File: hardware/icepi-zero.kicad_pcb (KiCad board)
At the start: 4 copper layers, 65 x 30 mm, 68 parts, among them J1 Micro_SD_Card_Det2, J2 Conn_02x20_Counter_Clockwise, J3 HDMI_C_1.3, J4 USB_C_Receptacle_USB2.0_14P, J5 USB_C_Receptacle_USB2.0_14P, J6 USB_C_Receptacle_USB2.0_14P, U1 ECP5U_12_CABGA256, U10 TPD2EUSB30A, U11 W25Q128JVS, U2 TLV62569DBV, U3 TLV62569DBV, U4 TLV62569DBV, U5 PCA9306DC1, U6 FT231XQ, U7 W9825G6KH, U8 TPD2EUSB30A, U9 TPD2EUSB30A, Y1 YSO690PR

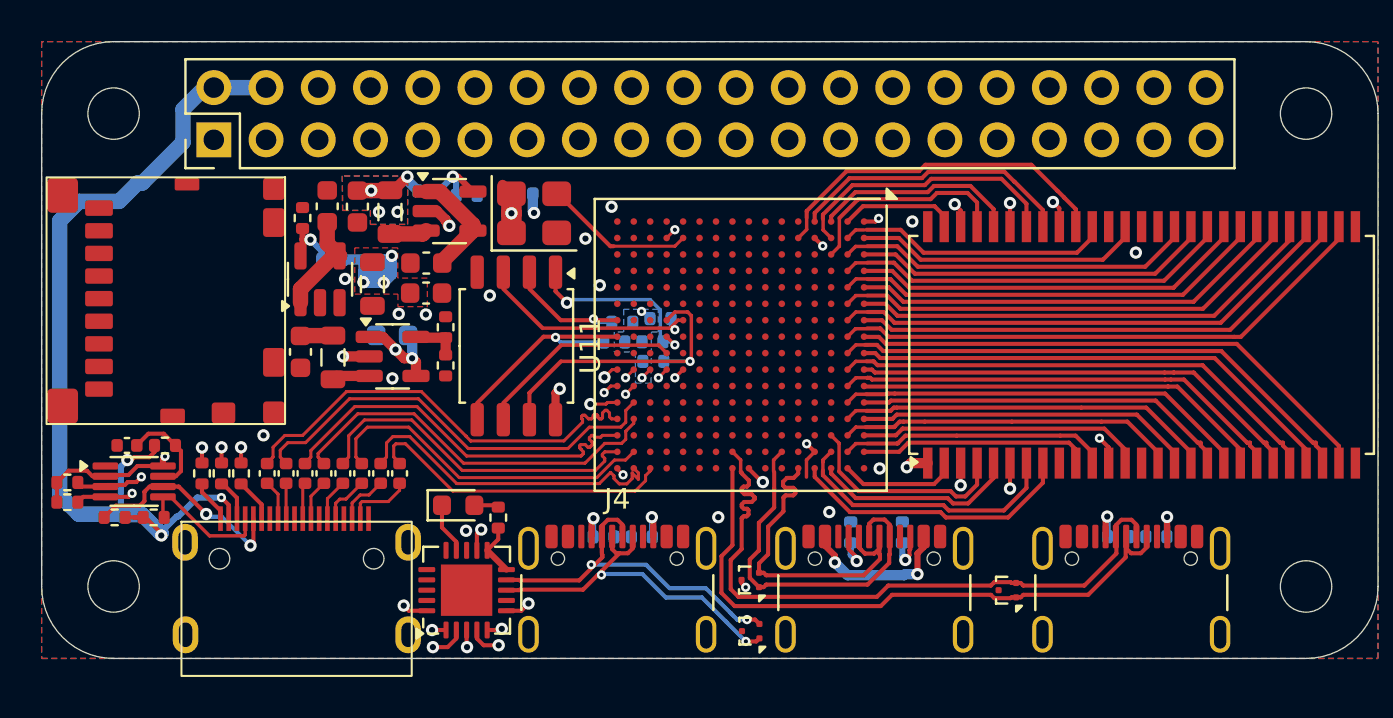
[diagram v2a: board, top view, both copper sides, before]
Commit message: Added the decoupling capacitors
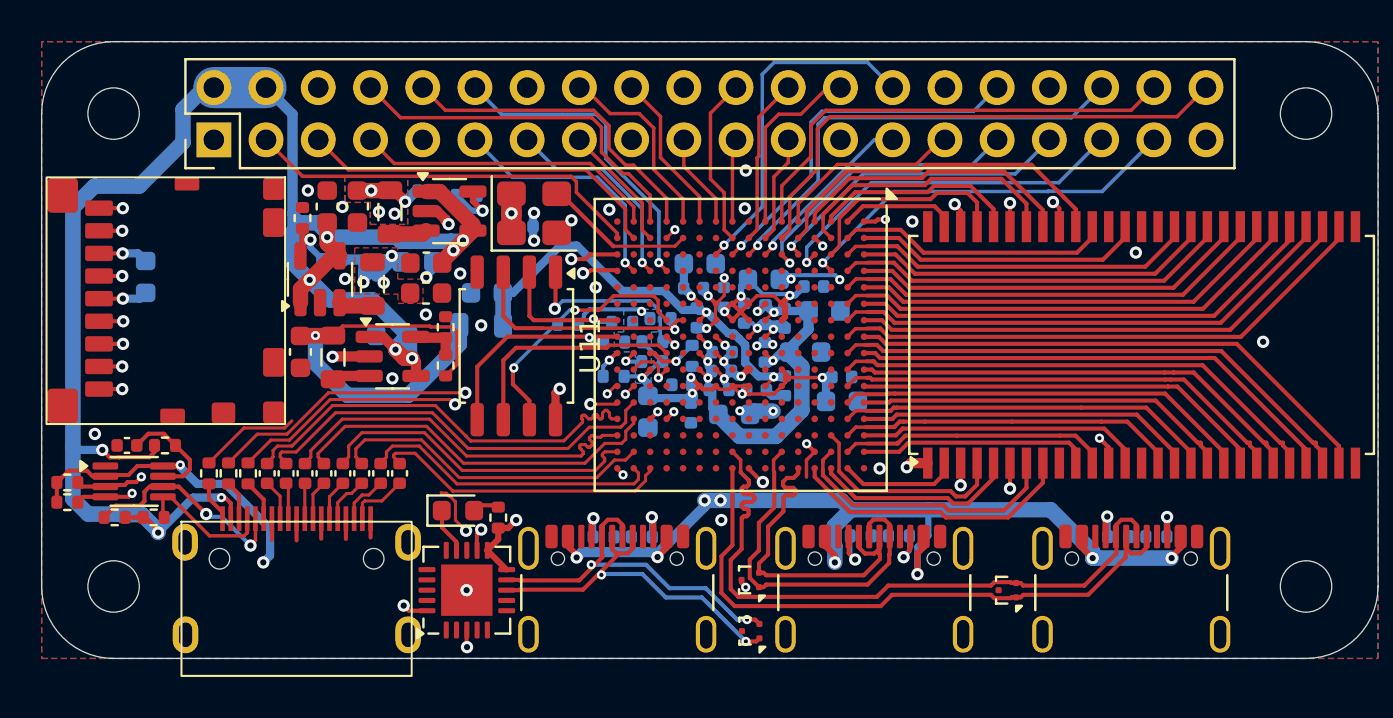
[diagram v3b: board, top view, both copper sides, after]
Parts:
- added C17: 10uF, Capacitor_SMD:C_0603_1608Metric, B.Cu at (137.7, 102.2)
- added C18: 100nF, Capacitor_SMD:C_0402_1005Metric, B.Cu at (152.2, 106.7)
- added C19: 100nF, Capacitor_SMD:C_0402_1005Metric, B.Cu at (147.9, 103.4)
- added C20: 22uF, Capacitor_SMD:C_0603_1608Metric, B.Cu at (134.3, 100.7)
- added C21: 10uF, Capacitor_SMD:C_0603_1608Metric, B.Cu at (154.1, 103.1)
- added C22: 10uF, Capacitor_SMD:C_0603_1608Metric, B.Cu at (153.1, 105.1)
- added C23: 10uF, Capacitor_SMD:C_0603_1608Metric, B.Cu at (149.7, 108.1)
- added C24: 100nF, Capacitor_SMD:C_0402_1005Metric, B.Cu at (152.1, 103.5)
- added C25: 100nF, Capacitor_SMD:C_0402_1005Metric, B.Cu at (151.2, 103.3)
- added C26: 100nF, Capacitor_SMD:C_0402_1005Metric, B.Cu at (151.2, 105.1)
- added C27: 100nF, Capacitor_SMD:C_0402_1005Metric, B.Cu at (148.9, 106.9)
- added C28: 100nF, Capacitor_SMD:C_0402_1005Metric, B.Cu at (149.1, 106.0)
- added C29: 100nF, Capacitor_SMD:C_0402_1005Metric, B.Cu at (149.1, 105.1)
- added C30: 10uF, Capacitor_SMD:C_0603_1608Metric, B.Cu at (145.5, 108.0)
- added C31: 100nF, Capacitor_SMD:C_0402_1005Metric, B.Cu at (147.1, 106.7)
- added C32: 100nF, Capacitor_SMD:C_0402_1005Metric, B.Cu at (147.6, 108.1)
- added C33: 10uF, Capacitor_SMD:C_0603_1608Metric, B.Cu at (148.0, 100.8)
- added C34: 100nF, Capacitor_SMD:C_0402_1005Metric, B.Cu at (147.7, 102.0)
- added C35: 10uF, Capacitor_SMD:C_0603_1608Metric, B.Cu at (151.1, 101.6)
- added C36: 100nF, Capacitor_SMD:C_0402_1005Metric, B.Cu at (149.2, 102.4)
- added C37: 100nF, Capacitor_SMD:C_0402_1005Metric, B.Cu at (153.6, 101.9)
- added C38: 100nF, Capacitor_SMD:C_0402_1005Metric, B.Cu at (150.2, 103.2)
- added C39: 100nF, Capacitor_SMD:C_0402_1005Metric, B.Cu at (154.9, 106.3)
- added C40: 100nF, Capacitor_SMD:C_0402_1005Metric, B.Cu at (150.8, 106.9)
- added C41: 10uF, Capacitor_SMD:C_0603_1608Metric, B.Cu at (154.9, 107.5)
- added C42: 10uF, Capacitor_SMD:C_0603_1608Metric, B.Cu at (121.1, 101.4)
- added FB1: 100R@100MHz, Inductor_SMD:L_0805_2012Metric, B.Cu at (137.4, 103.8)
- added R27: 15k, Resistor_SMD:R_0402_1005Metric, B.Cu at (145.7, 105.6)
- added R28: 15k, Resistor_SMD:R_0402_1005Metric, B.Cu at (147.6, 105.3)
- added R29: 15k, Resistor_SMD:R_0402_1005Metric, B.Cu at (143.8, 106.3)
- C6: value 22uF -> 10uF
- J3: footprint cyao:XKB Connection A71-05H4-111N1 -> icepi-lib:XKB Connection A71-05H4-111N1
- moved R25 4.51 mm to (141.6, 103.8), turned to 180 degrees
- moved C16 1.59 mm to (139.4, 99.0)
- moved R17 0.52 mm to (155.8, 114.0), turned to 0 degrees
- moved R7 0.34 mm to (126.0, 111.0)
- moved R8 0.34 mm to (125.1, 111.0)
- moved R9 0.34 mm to (124.1, 111.0)
- moved D1 0.26 mm to (136.2, 112.8)
- moved R18 0.24 mm to (157.7, 114.0), turned to 0 degrees
- turned L1 to -90 degrees
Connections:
- J1 pad 1: unconnected-(J1-DAT2-Pad1) -> DAT2
- J1 pad 10: unconnected-(J1-DET_A-Pad10) -> DET
- J1 pad 11: unconnected-(J1-SHIELD-Pad11) -> GND
- J1 pad 2: unconnected-(J1-DAT3/CD-Pad2) -> DAT3
- J1 pad 3: unconnected-(J1-CMD-Pad3) -> CMD
- J1 pad 4: unconnected-(J1-VDD-Pad4) -> +3V3
- J1 pad 5: unconnected-(J1-CLK-Pad5) -> CLK
- J1 pad 6: unconnected-(J1-VSS-Pad6) -> GND
- J1 pad 7: unconnected-(J1-DAT0-Pad7) -> DAT0
- J1 pad 8: unconnected-(J1-DAT1-Pad8) -> DAT1
- J1 pad 9: unconnected-(J1-DET_B-Pad9) -> GND
- J2 pad 10: unconnected-(J2-Pin_10-Pad10) -> GPIO_10
- J2 pad 11: unconnected-(J2-Pin_11-Pad11) -> GPIO_11
- J2 pad 12: unconnected-(J2-Pin_12-Pad12) -> GPIO_12
- J2 pad 13: unconnected-(J2-Pin_13-Pad13) -> GPIO_13
- J2 pad 15: unconnected-(J2-Pin_15-Pad15) -> GPIO_15
- J2 pad 16: unconnected-(J2-Pin_16-Pad16) -> GPIO_16
- J2 pad 18: unconnected-(J2-Pin_18-Pad18) -> GPIO_18
- J2 pad 19: unconnected-(J2-Pin_19-Pad19) -> GPIO_19
- J2 pad 21: unconnected-(J2-Pin_21-Pad21) -> GPIO_21
- J2 pad 22: unconnected-(J2-Pin_22-Pad22) -> GPIO_22
- J2 pad 23: unconnected-(J2-Pin_23-Pad23) -> GPIO_23
- J2 pad 24: unconnected-(J2-Pin_24-Pad24) -> GPIO_24
- J2 pad 26: unconnected-(J2-Pin_26-Pad26) -> GPIO_26
- J2 pad 27: unconnected-(J2-Pin_27-Pad27) -> GPIO_27
- J2 pad 28: unconnected-(J2-Pin_28-Pad28) -> GPIO_28
- J2 pad 29: unconnected-(J2-Pin_29-Pad29) -> GPIO_29
- J2 pad 3: unconnected-(J2-Pin_3-Pad3) -> GPIO_3
- J2 pad 31: unconnected-(J2-Pin_31-Pad31) -> GPIO_31
- J2 pad 32: unconnected-(J2-Pin_32-Pad32) -> GPIO_32
- J2 pad 33: unconnected-(J2-Pin_33-Pad33) -> GPIO_33
- J2 pad 35: unconnected-(J2-Pin_35-Pad35) -> GPIO_35
- J2 pad 36: unconnected-(J2-Pin_36-Pad36) -> GPIO_36
- J2 pad 37: unconnected-(J2-Pin_37-Pad37) -> GPIO_37
- J2 pad 38: unconnected-(J2-Pin_38-Pad38) -> GPIO_38
- J2 pad 40: unconnected-(J2-Pin_40-Pad40) -> GPIO_40
- J2 pad 5: unconnected-(J2-Pin_5-Pad5) -> GPIO_5
- J2 pad 7: unconnected-(J2-Pin_7-Pad7) -> GPIO_7
- J2 pad 8: unconnected-(J2-Pin_8-Pad8) -> GPIO_8
- U1 pad C4: unconnected-(U1B-PT11A/+-PadC4) -> GPIO_37
- U1 pad D3: unconnected-(U1G-PL2D/-/LDQ8-PadD3) -> GPIO_35
- U1 pad E1: unconnected-(U1G-PL11D/-/LDQ8-PadE1) -> GPIO_29
- U1 pad E3: unconnected-(U1G-PL5C/+/LDQ8-PadE3) -> GPIO_33
- U1 pad F1: unconnected-(U1G-PL14A/+/HS/LDQ20-PadF1) -> GPIO_38
- U1 pad F10: Net-(U1C-VCCIO1[2]-PadF10) -> +3V3
- U1 pad F11: Net-(U1C-VCCIO1[2]-PadF10) -> +3V3
- U1 pad F2: unconnected-(U1G-PL11C/+/LDQ8-PadF2) -> GPIO_40
- U1 pad F3: unconnected-(U1G-PL5D/-/LDQ8-PadF3) -> GPIO_31
- U1 pad F6: Net-(U1B-VCCIO0[2]-PadF6) -> +3V3
- U1 pad F7: Net-(U1B-VCCIO0[2]-PadF6) -> +3V3
- U1 pad G1: unconnected-(U1G-PL20A/+/GR_PCLK7_1/HS/LDQS20-PadG1) -> GPIO_26
- U1 pad G2: unconnected-(U1G-PL14B/-/HS/LDQ20-PadG2) -> GPIO_23
- U1 pad G3: unconnected-(U1G-PL14C/+/VREF1_7/LDQ20-PadG3) -> GPIO_27
- U1 pad G6: Net-(U1A-VCC[6]-PadG6) -> +1V1
- U1 pad G7: Net-(U1A-VCC[6]-PadG6) -> +1V1
- U1 pad G9: Net-(U1A-VCC[6]-PadG6) -> +1V1
- U1 pad H11: Net-(U1D-VCCIO2[2]-PadH11) -> +3V3
- U1 pad H2: unconnected-(U1G-PL20B/-/HS/LDQSN20-PadH2) -> GPIO_24
- U1 pad H3: unconnected-(U1G-PL14D/-/LDQ20-PadH3) -> GPIO_36
- U1 pad H6: Net-(U1G-VCCIO7[2]-PadH6) -> +3V3
- U1 pad H7: Net-(U1G-VCCIO7[2]-PadH6) -> +3V3
- U1 pad J1: unconnected-(U1G-PL23A/+/PCLKT7_1/HS/LDQ20-PadJ1) -> GPIO_21
- U1 pad J11: Net-(U1D-VCCIO2[2]-PadH11) -> +3V3
- U1 pad J2: unconnected-(U1G-PL23B/-/PCLKC7_1/HS/LDQ20-PadJ2) -> GPIO_22
- U1 pad J3: unconnected-(U1G-PL20C/+/GR_PCLK7_0/LDQ20-PadJ3) -> GPIO_32
- U1 pad J6: Net-(U1F-VCCIO6[2]-PadJ6) -> +3V3
- U1 pad J7: Net-(U1F-VCCIO6[2]-PadJ6) -> +3V3
- U1 pad K1: unconnected-(U1G-PL23C/+/PCLKT7_0/LDQ20-PadK1) -> GPIO_19
- U1 pad K11: Net-(U1E-VCCIO3[2]-PadK11) -> +3V3
- U1 pad K3: unconnected-(U1G-PL20D/-/LDQ20-PadK3) -> GPIO_28
- U1 pad L1: unconnected-(U1F-PL26A/+/PCLKT6_1/HS/LDQ32-PadL1) -> GPIO_18
- U1 pad L10: Net-(U1A-VCC[6]-PadG6) -> +1V1
- U1 pad L11: Net-(U1E-VCCIO3[2]-PadK11) -> +3V3
- U1 pad L6: unconnected-(U1H-VCCIO8-PadL6) -> +3V3
- U1 pad L8: Net-(U1A-VCC[6]-PadG6) -> +1V1
- U1 pad L9: Net-(U1A-VCC[6]-PadG6) -> +1V1
- U1 pad M1: unconnected-(U1F-PL26C/+/PCLKT6_0/LDQ32-PadM1) -> GPIO_16
- U1 pad N1: unconnected-(U1F-PL32A/+/HS/LDQS32-PadN1) -> GPIO_10
- U1 pad N4: unconnected-(U1F-PL38A/+/HS/LDQ44-PadN4) -> GPIO_12
- U1 pad P1: unconnected-(U1F-PL35A/+/HS/LDQ32-PadP1) -> GPIO_8
- U1 pad P2: unconnected-(U1F-PL32B/-/HS/LDQSN32-PadP2) -> GPIO_15
- U1 pad P4: unconnected-(U1F-PL41A/+/HS/LDQ44-PadP4) -> GPIO_13
- U1 pad P9: unconnected-(U1H-DONE-PadP9) -> DONE
- U1 pad R1: unconnected-(U1F-PL35B/-/VREF1_6/HS/LDQ32-PadR1) -> GPIO_7
- U1 pad R2: unconnected-(U1F-PL38C/+/LDQ44-PadR2) -> GPIO_5
- U1 pad R4: unconnected-(U1F-PL41C/+/LDQ44-PadR4) -> GPIO_11
- U1 pad R9: unconnected-(U1H-PROGRAMN-PadR9) -> PROGRAMMING
- U1 pad T2: unconnected-(U1F-PL38D/-/LDQ44-PadT2) -> GPIO_3
- U1 pad T3: unconnected-(U1F-PL41D/-/LDQ44-PadT3) -> FPDI_SCL
- U1 pad T4: unconnected-(U1F-PL44B/-/HS/LDQSN44-PadT4) -> FPDI_SDA
- U1 pad T9: unconnected-(U1H-INITN-PadT9) -> INITN
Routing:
- net +5V: track 68.9 -> 200.2 mm, vias 8 -> 18
- net +1V1: track 10.2 -> 61.4 mm, vias 3 -> 9
- net +3V3: track 19.8 -> 66.6 mm, vias 12 -> 22
- net GND: track 18.0 -> 51.2 mm, vias 33 -> 55
- net GPIO_40: track 0.00 -> 25.8 mm
- net GPIO_38: track 0.00 -> 22.7 mm
- net GPIO_36: track 0.00 -> 22.3 mm, vias 0 -> 1
- net Net-(C17-Pad1): track 0.00 -> 21.3 mm, vias 0 -> 2
- net +2V5: track 1.59 -> 21.2 mm, vias 0 -> 1
- net GPIO_3: track 0.00 -> 19.5 mm
- net GPIO_37: track 0.00 -> 19.2 mm, vias 0 -> 1
- net GPIO_5: track 0.00 -> 17.9 mm
- net GPIO_35: track 0.00 -> 17.8 mm, vias 0 -> 1
- net GPIO_32: track 0.00 -> 17.8 mm, vias 0 -> 1
- net GPIO_8: track 0.00 -> 17.8 mm
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
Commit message: V1.0 Final Revision and Readme documentation
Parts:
- added C30: 100nF, Capacitor_SMD:C_0402_1005Metric, F.Cu at (179.8, 112.0)
- added C31: 100nF, Capacitor_SMD:C_0402_1005Metric, B.Cu at (168.6, 111.2)
- added C32: 100nF, Capacitor_SMD:C_0402_1005Metric, B.Cu at (166.7, 111.2)
- added C33: 10uF, Capacitor_SMD:C_0603_1608Metric, B.Cu at (161.9, 110.4)
- added C34: 100nF, Capacitor_SMD:C_0402_1005Metric, B.Cu at (161.9, 111.6)
- added C35: 100nF, Capacitor_SMD:C_0402_1005Metric, F.Cu at (169.1, 97.5)
- added D1: WHITE, LED_SMD:LED_0603_1608Metric, F.Cu at (168.2, 112.2)
- added D2: WHITE, LED_SMD:LED_0603_1608Metric, F.Cu at (174.1, 112.2)
- added D3: WHITE, LED_SMD:LED_0603_1608Metric, F.Cu at (177.1, 112.2)
- added D4: WHITE, LED_SMD:LED_0603_1608Metric, F.Cu at (171.1, 112.3)
- added G***: LOGO, LOGO, B.Cu at (178.1, 99.0)
- added R1: 470, Resistor_SMD:R_0402_1005Metric, B.Cu at (168.3, 112.3)
- added R2: 470, Resistor_SMD:R_0402_1005Metric, B.Cu at (174.6, 112.2)
- added R3: 470, Resistor_SMD:R_0402_1005Metric, B.Cu at (177.2, 112.2)
- added R4: 470, Resistor_SMD:R_0402_1005Metric, B.Cu at (171.4, 112.2)
- added TP1: TestPoint, TestPoint:TestPoint_Pad_D2.0mm, B.Cu at (117.9, 107.6)
- added TP2: TestPoint, TestPoint:TestPoint_Pad_D2.0mm, B.Cu at (132.6, 97.8)
- added TP3: TestPoint, TestPoint:TestPoint_Pad_D2.0mm, B.Cu at (128.8, 105.2)
- added TP4: TestPoint, TestPoint:TestPoint_Pad_D2.0mm, B.Cu at (173.8, 101.6)
- added TP5: TestPoint, TestPoint:TestPoint_Pad_D2.0mm, B.Cu at (129.1, 115.5)
- added TP6: TestPoint, TestPoint:TestPoint_Pad_D2.0mm, B.Cu at (136.6, 106.2)
- added TP7: TestPoint, TestPoint:TestPoint_Pad_D2.0mm, B.Cu at (153.9, 117.5)
- added TP8: TestPoint, TestPoint:TestPoint_Pad_D2.0mm, B.Cu at (144.9, 118.1)
- C13: renamed from C3; moved to F.Cu
- C3: renamed from C20; moved to F.Cu
- R6: renamed from R2; moved to B.Cu
- R8: renamed from R4; moved to B.Cu
- Y1: value YSO690PR -> SIT8008xx-1x-xxE-100.000000; footprint Oscillator:Oscillator_SMD_SiT_PQFN-4Pin_3.2x2.5mm -> Oscillator:Oscillator_SMD_SiT_PQFN-4Pin_2.5x2.0mm
- moved C3 7.47 mm to (129.1, 106.1), turned to 180 degrees
- moved C2 6.07 mm to (129.1, 104.6), turned to 180 degrees
- moved C14 5.82 mm to (134.3, 106.3), turned to 0 degrees
- moved R6 5.03 mm to (126.7, 103.2), turned to 180 degrees
- moved R8 4.21 mm to (131.9, 105.8)
- moved C13 3.89 mm to (134.7, 100.8)
- moved R7 3.86 mm to (131.8, 106.4), turned to 180 degrees
- moved R5 3.02 mm to (128.6, 103.2)
- moved L1 3.01 mm to (129.3, 103.0), turned to 0 degrees
- moved C18 2.75 mm to (132.0, 101.0), turned to -90 degrees
- moved R33 2.29 mm to (141.8, 105.2), turned to -90 degrees
- moved U2 2.25 mm to (134.5, 103.6), turned to -90 degrees
- moved L2 2.12 mm to (131.9, 104.2), turned to -90 degrees
- moved U1 1.47 mm to (129.5, 100.1)
- moved R24 1.21 mm to (169.5, 115.0), turned to 90 degrees
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- renumbered C27 to C10, C28 to C11, C29 to C12, C4 to C14, C17 to C15, C18 to C16, C19 to C17, C5 to C18, C6 to C19, C16 to C20, C7 to C21, C8 to C22, C9 to C23, C10 to C24, C11 to C25, C12 to C26, C13 to C27, C14 to C28, C15 to C29, C33 to C36, C34 to C37, C42 to C38, C38 to C39, C23 to C4, C41 to C40, C39 to C41, C37 to C42, C40 to C43, C30 to C44, C31 to C45, C32 to C46, C35 to C47, C36 to C48, C22 to C5, C21 to C6, C24 to C7, C25 to C8, C26 to C9, D1 to D5, J2 to J1, J3 to J2, J4 to J3, J6 to J4, J1 to J6, R6 to R10, R10 to R11, R11 to R12, R12 to R13, R13 to R14, R14 to R15, R7 to R16, R8 to R17, R9 to R18, R15 to R19, R16 to R20, R19 to R22, R17 to R23, R20 to R24, R18 to R25, R22 to R26, R23 to R27, R24 to R28, R25 to R29, R26 to R30, R27 to R31, R28 to R32, R29 to R33, R1 to R5, R3 to R7, R5 to R9, U2 to U1, U7 to U10, U3 to U2, U1 to U3, U8 to U7, U10 to U8
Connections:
- net Net-(C17-Pad1) renamed /Power/FILTERED_2V5
- J6 pad 1: DAT2 -> SD_DAT2
- J6 pad 10: DET -> SD_DET
- J6 pad 2: DAT3 -> SD_DAT3
- J6 pad 3: CMD -> SD_CMD
- J6 pad 5: CLK -> SD_CLK
- J6 pad 7: DAT0 -> SD_DAT0
- J6 pad 8: DAT1 -> SD_DAT1
- U3 pad C13: unconnected-(U1C-PT60B/--PadC13) -> LED3
- U3 pad D14: unconnected-(U1D-PR2D/-/RDQ8-PadD14) -> LED2
- U3 pad E15: unconnected-(U1D-PR8B/-/HS/RDQSN8-PadE15) -> LED4
- U3 pad F16: unconnected-(U1D-PR14A/+/HS/RDQ20-PadF16) -> LED1
- U3 pad K15: unconnected-(U1D-PR23D/-/PCLKC2_0/RDQ20-PadK15) -> USB_RXD
- U3 pad K16: unconnected-(U1D-PR23C/+/PCLKT2_0/RDQ20-PadK16) -> USB_TXD
- U3 pad L14: unconnected-(U1E-PR32C/+/RDQ32-PadL14) -> FPDI_HPD
- U3 pad L15: unconnected-(U1E-PR26B/-/PCLKC3_1/HS/RDQ32-PadL15) -> ~{USB_DTR}
- U3 pad L16: unconnected-(U1E-PR26A/+/PCLKT3_1/HS/RDQ32-PadL16) -> ~{USB_RTS}
- U3 pad M14: unconnected-(U1E-PR32D/-/RDQ32-PadM14) -> SD_DAT3
- U3 pad M15: unconnected-(U1E-PR26D/-/PCLKC3_0/RDQ32-PadM15) -> SD_DAT2
- U3 pad M16: unconnected-(U1E-PR26C/+/PCLKT3_0/RDQ32-PadM16) -> SD_DET
- U3 pad N16: unconnected-(U1E-PR32A/+/HS/RDQS32-PadN16) -> SD_CLK
- U3 pad P14: unconnected-(U1E-PR38B/-/HS/RDQ44-PadP14) -> SD_DAT0
- U3 pad P15: unconnected-(U1E-PR32B/-/HS/RDQSN32-PadP15) -> SD_CMD
- U3 pad P3: unconnected-(U1F-PL38B/-/HS/LDQ44-PadP3) -> GPIO_13
- U3 pad P4: GPIO_13 -> unconnected-(U3F-PL41A/+/HS/LDQ44-PadP4)
- U3 pad P5: unconnected-(U1F-PL47D/-/LLC_GPLL0C_IN/LDQ44-PadP5) -> FPDI_UTIL
- U3 pad R14: unconnected-(U1E-PR41B/-/HS/RDQ44-PadR14) -> SD_DAT1
- U3 pad R3: unconnected-(U1F-PL41B/-/HS/LDQ44-PadR3) -> GPIO_11
- U3 pad R4: GPIO_11 -> unconnected-(U3F-PL41C/+/LDQ44-PadR4)
- U3 pad R5: unconnected-(U1F-PL44A/+/HS/LDQS44-PadR5) -> FPDI_CEC
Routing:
- net SD_DAT0: track 0.00 -> 35.9 mm, vias 0 -> 2
- net SD_DAT1: track 0.00 -> 35.3 mm, vias 0 -> 2
- net SD_CLK: track 0.00 -> 34.5 mm, vias 0 -> 2
- net JTAG_TCK: track 0.00 -> 33.9 mm, vias 0 -> 2
- net SD_DAT3: track 0.00 -> 33.5 mm, vias 0 -> 2
- net FPDI_SDA: track 4.56 -> 37.8 mm, vias 2 -> 4
- net SD_DAT2: track 0.00 -> 32.9 mm, vias 0 -> 2
- net FPDI_SCL: track 5.70 -> 38.3 mm, vias 2 -> 4
- net SD_DET: track 0.00 -> 32.4 mm, vias 0 -> 2
- net SD_CMD: track 0.00 -> 31.9 mm, vias 0 -> 2
- net JTAG_TMS: track 0.65 -> 32.3 mm, vias 1 -> 3
- net JTAG_TDI: track 0.58 -> 31.2 mm, vias 1 -> 2
- net +3V3: track 66.6 -> 93.0 mm, vias 22 -> 25
- net USB_TXD: track 0.00 -> 25.2 mm, vias 0 -> 2
- net LED3: track 0.00 -> 24.8 mm, vias 0 -> 1
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- added copper zone on In2.Cu, net +1V1
- added copper zone on B.Cu, net +2V5
- added copper zone on F.Cu, net +2V5
- added copper zone on In2.Cu, net +5V
- added copper zone on B.Cu, net /Power/FILTERED_2V5

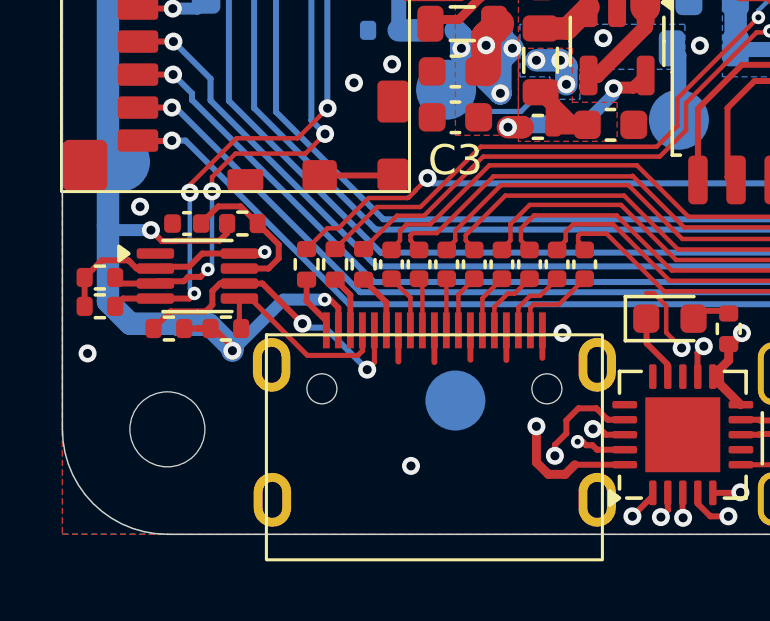
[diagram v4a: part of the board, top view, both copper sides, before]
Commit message: Fix level shifter EN voltage error
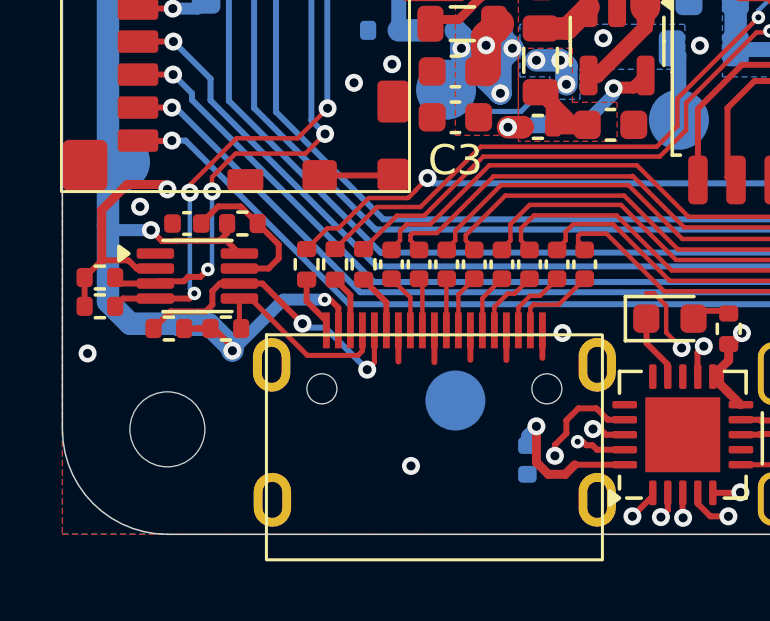
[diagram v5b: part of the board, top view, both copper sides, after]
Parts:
- added C49: 100nF, Capacitor_SMD:C_0402_1005Metric, B.Cu at (131.5, 117.5)
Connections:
- U5 pad 8: +3V3 -> +5V
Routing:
- net +5V: track 200.9 -> 202.0 mm
- net Net-(U6-3V3OUT): track 15.7 -> 16.5 mm

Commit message: Add a revision
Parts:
- added C50: 100nF, Capacitor_SMD:C_0402_1005Metric, B.Cu at (131.0, 102.5)
- added C51: 100nF, Capacitor_SMD:C_0402_1005Metric, B.Cu at (135.0, 102.8)
- added C52: 100nF, Capacitor_SMD:C_0402_1005Metric, B.Cu at (139.5, 97.2)
- R10: value 18k -> 3.3k
- R5: value 15k -> 10k
- R6: value 18k -> 12k
- R8: value 18k -> 4.7k
- moved R9 0.84 mm to (136.2, 97.2), turned to -90 degrees
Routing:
- net +3V3: track 93.4 -> 91.5 mm
- net GND: track 69.6 -> 68.2 mm
- net Net-(U4-FB): track 3.65 -> 2.75 mm

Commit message: Pre-prod fixes
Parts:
- added D6: WHITE, LED_SMD:LED_0603_1608Metric, F.Cu at (178.3, 112.2)
- added R34: 470, Resistor_SMD:R_0402_1005Metric, B.Cu at (178.4, 112.2)
- added R35: 4.7k, Resistor_SMD:R_0402_1005Metric, B.Cu at (142.8, 106.0)
- added R36: 4.7k, Resistor_SMD:R_0402_1005Metric, B.Cu at (144.3, 108.0)
- added R37: 4.7k, Resistor_SMD:R_0402_1005Metric, B.Cu at (150.3, 109.3)
- added R38: 4.7k, Resistor_SMD:R_0402_1005Metric, B.Cu at (137.3, 118.3)
- added TP10: TestPoint, TestPoint:TestPoint_Pad_D2.0mm, B.Cu at (157.8, 104.5)
- added TP9: TestPoint, TestPoint:TestPoint_Pad_D2.0mm, B.Cu at (157.8, 100.8)
- moved R29 2.70 mm to (140.5, 106.2), turned to 90 degrees
- moved C32 2.21 mm to (165.9, 113.2)
- moved C43 1.78 mm to (152.5, 107.2)
- moved D1 1.77 mm to (166.4, 112.2)
- moved D4 1.77 mm to (169.4, 112.3)
- moved R1 1.77 mm to (166.6, 112.3)
- moved D2 1.77 mm to (172.4, 112.2)
- moved D3 1.77 mm to (175.4, 112.2)
- moved R2 1.77 mm to (172.9, 112.2)
- moved R3 1.77 mm to (175.4, 112.2)
- moved R4 1.77 mm to (169.7, 112.2)
- moved TP6 1.40 mm to (137.9, 106.2)
- moved R8 1.10 mm to (132.8, 106.4), turned to -90 degrees
- moved R33 0.85 mm to (141.9, 106.0)
- moved C16 0.74 mm to (152.8, 106.3), turned to 0 degrees
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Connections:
- R2 pad 1: LED2 -> LED3
- R3 pad 1: LED3 -> LED4
- R4 pad 1: LED4 -> LED2
- U3 pad C13: LED3 -> LED4
- U3 pad C4: GPIO_37 -> unconnected-(U3B-PT11A/+-PadC4)
- U3 pad C7: unconnected-(U3B-PT27A/+/PCLKT0_1-PadC7) -> Net-(U3B-PT27A/+/PCLKT0_1)
- U3 pad C8: unconnected-(U3C-PT35A/+/PCLKT1_0-PadC8) -> Net-(U3C-PT35A/+/PCLKT1_0)
- U3 pad D13: unconnected-(U3C-PT62A/+-PadD13) -> LED5
- U3 pad D14: LED2 -> LED3
- U3 pad D3: GPIO_35 -> unconnected-(U3G-PL2D/-/LDQ8-PadD3)
- U3 pad D4: unconnected-(U3B-PT9B/--PadD4) -> GPIO_37
- U3 pad E15: LED4 -> LED2
- U3 pad E4: unconnected-(U3B-PT9A/+-PadE4) -> GPIO_35
- U3 pad K1: GPIO_19 -> unconnected-(U3G-PL23C/+/PCLKT7_0/LDQ20-PadK1)
- U3 pad L2: unconnected-(U3F-PL26B/-/PCLKC6_1/HS/LDQ32-PadL2) -> GPIO_19
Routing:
- net LED5: track 0.00 -> 27.8 mm, vias 0 -> 1
- net +5V: track 202.0 -> 224.2 mm
- net +1V1: track 48.4 -> 39.2 mm, vias 10 -> 11
- net GND: track 68.2 -> 76.7 mm, vias 71 -> 78
- net Net-(U3B-PT27A/+/PCLKT0_1): track 0.00 -> 5.95 mm, vias 0 -> 1
- net Net-(U3C-PT35A/+/PCLKT1_0): track 0.00 -> 3.60 mm, vias 0 -> 1
- net LED3: track 24.8 -> 22.5 mm
- net LED1: track 19.2 -> 17.3 mm
- net Net-(D6-A): track 0.00 -> 1.59 mm, vias 0 -> 1
- net FLASH_CLK: track 12.3 -> 10.8 mm
- net Net-(U6-3V3OUT): track 16.5 -> 15.0 mm
- net JTAG_TMS: track 32.3 -> 33.5 mm
- net +3V3: track 91.5 -> 92.6 mm, vias 25 -> 27
- net LED2: track 23.2 -> 22.2 mm
- net GPIO_19: track 4.62 -> 5.42 mm
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- added copper zone on B.Cu, net +1V1
